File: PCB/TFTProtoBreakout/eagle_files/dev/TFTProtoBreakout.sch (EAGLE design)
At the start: 13 parts, among them SW1 PCM12SMTR, SW2 PCM12SMTR, SW3 PCM12SMTR, SW4 PCM12SMTR

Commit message: Added first cut of trace routing to board design. A bit messy, but functional.
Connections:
- removed net LEDA: C1.1, JP1.20, JP2.1, JP7.2
- net VCC: now also C1.1, JP1.20, JP2.1, JP7.2
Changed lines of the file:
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@@
-</segment>
-</net>
-<net name="LEDA" class="0">
-<segment>
-<pinref part="JP2" gate="G$1" pin="1"/>
-<wire x1="43.18" y1="5.08" x2="35.56" y2="5.08" width="0.1524" layer="91"/>
-<wire x1="35.56" y1="5.08" x2="35.56" y2="20.32" width="0.1524" layer="91"/>
-<pinref part="JP1" gate="G$1" pin="20"/>
-<wire x1="43.18" y1="22.86" x2="38.1" y2="22.86" width="0.1524" layer="91"/>
-<wire x1="38.1" y1="22.86" x2="38.1" y2="20.32" width="0.1524" layer="91"/>
-<wire x1="38.1" y1="20.32" x2="38.1" y2="17.78" width="0.1524" layer="91"/>
-<wire x1="38.1" y1="17.78" x2="63.5" y2="17.78" width="0.1524" layer="91"/>
-<wire x1="63.5" y1="17.78" x2="63.5" y2="22.86" width="0.1524" layer="91"/>
-<wire x1="63.5" y1="22.86" x2="81.28" y2="22.86" width="0.1524" layer="91"/>
-<wire x1="81.28" y1="22.86" x2="81.28" y2="20.32" width="0.1524" layer="91"/>
-<pinref part="JP7" gate="G$1" pin="2"/>
-<wire x1="81.28" y1="20.32" x2="81.28" y2="15.24" width="0.1524" layer="91"/>
-<wire x1="81.28" y1="15.24" x2="76.2" y2="15.24" width="0.1524" layer="91"/>
-<wire x1="35.56" y1="20.32" x2="38.1" y2="20.32" width="0.1524" layer="91"/>
-<pinref part="C1" gate="G$1" pin="1"/>
-<wire x1="88.9" y1="17.78" x2="88.9" y2="20.32" width="0.1524" layer="91"/>
-<wire x1="88.9" y1="20.32" x2="81.28" y2="20.32" width="0.1524" layer="91"/>
 </segment>
 </net>
@@
 <wire x1="-38.1" y1="-10.16" x2="-45.72" y2="-10.16" width="0.1524" layer="91"/>
 </segment>
+<segment>
+<pinref part="JP2" gate="G$1" pin="1"/>
+<wire x1="43.18" y1="5.08" x2="35.56" y2="5.08" width="0.1524" layer="91"/>
+<wire x1="35.56" y1="5.08" x2="35.56" y2="20.32" width="0.1524" layer="91"/>
+<pinref part="JP1" gate="G$1" pin="20"/>
+<wire x1="43.18" y1="22.86" x2="38.1" y2="22.86" width="0.1524" layer="91"/>
+<wire x1="38.1" y1="22.86" x2="38.1" y2="20.32" width="0.1524" layer="91"/>
+<wire x1="38.1" y1="20.32" x2="38.1" y2="17.78" width="0.1524" layer="91"/>
+<wire x1="38.1" y1="17.78" x2="63.5" y2="17.78" width="0.1524" layer="91"/>
+<wire x1="63.5" y1="17.78" x2="63.5" y2="22.86" width="0.1524" layer="91"/>
+<wire x1="63.5" y1="22.86" x2="81.28" y2="22.86" width="0.1524" layer="91"/>
+<wire x1="81.28" y1="22.86" x2="81.28" y2="20.32" width="0.1524" layer="91"/>
+<pinref part="JP7" gate="G$1" pin="2"/>
+<wire x1="81.28" y1="20.32" x2="81.28" y2="15.24" width="0.1524" layer="91"/>
+<wire x1="81.28" y1="15.24" x2="76.2" y2="15.24" width="0.1524" layer="91"/>
+<wire x1="35.56" y1="20.32" x2="38.1" y2="20.32" width="0.1524" layer="91"/>
+<pinref part="C1" gate="G$1" pin="1"/>
+<wire x1="88.9" y1="17.78" x2="88.9" y2="20.32" width="0.1524" layer="91"/>
+<wire x1="88.9" y1="20.32" x2="81.28" y2="20.32" width="0.1524" layer="91"/>
+</segment>
 </net>

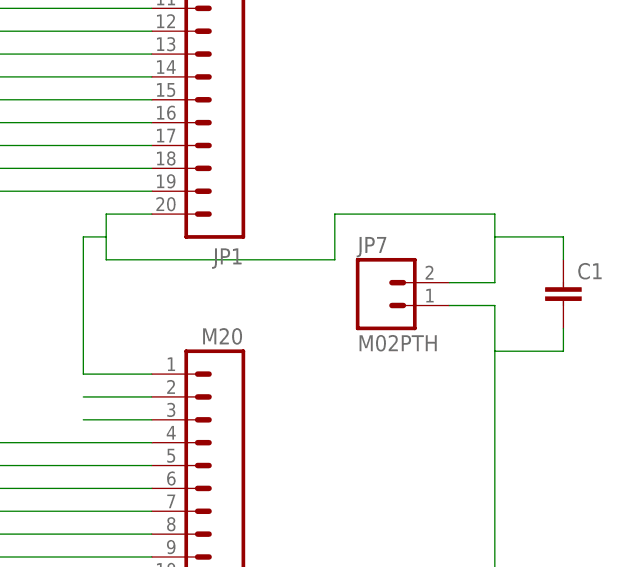
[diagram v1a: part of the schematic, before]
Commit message: Finalize routing to be more clean. Add keyhole for Power connections and Add labels.
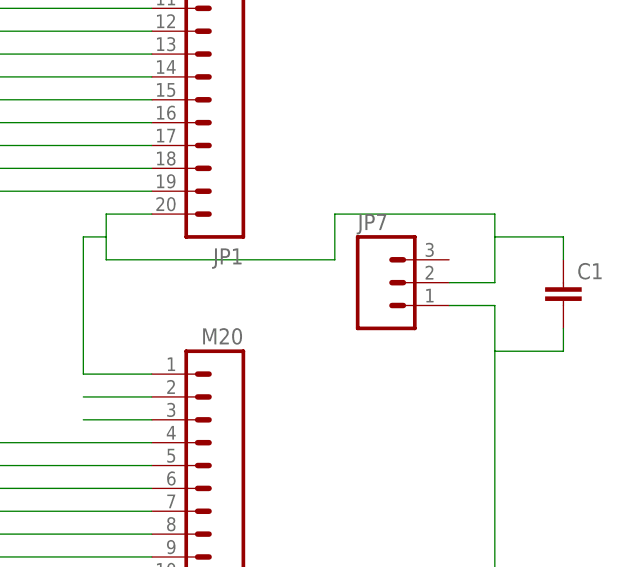
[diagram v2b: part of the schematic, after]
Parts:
- JP7: value M02PTH -> (none); device SparkFun-Connectors:M02PTH -> SparkFun-Connectors:M03PTH
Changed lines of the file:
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@@
 <part name="JP5" library="SparkFun-Connectors" deviceset="M03" device="PTH"/>
 <part name="JP6" library="SparkFun-Connectors" deviceset="M09" device=""/>
-<part name="JP7" library="SparkFun-Connectors" deviceset="M02" device="PTH"/>
 <part name="R1" library="SparkFun-Resistors" deviceset="1KOHM1/10W1%(0603)" device="" value="1K"/>
 <part name="SW1" library="freddyLibr" deviceset="PCM12SMTR" device=""/>
@@
 <part name="SW4" library="freddyLibr" deviceset="PCM12SMTR" device=""/>
 <part name="C1" library="SparkFun-Capacitors" deviceset="CAP" device="0805"/>
+<part name="JP7" library="SparkFun-Connectors" deviceset="M03" device="PTH"/>
 </parts>
 <sheets>
@@
 <instance part="JP5" gate="G$1" x="-15.24" y="-30.48"/>
 <instance part="JP6" gate="G$1" x="-2.54" y="-12.7"/>
-<instance part="JP7" gate="G$1" x="68.58" y="12.7"/>
 <instance part="R1" gate="G$1" x="30.48" y="71.12" rot="R180"/>
 <instance part="SW1" gate="G$1" x="-30.48" y="33.02" rot="R90"/>
@@
 <instance part="SW4" gate="G$1" x="-30.48" y="-12.7" rot="R90"/>
 <instance part="C1" gate="G$1" x="88.9" y="12.7"/>
+<instance part="JP7" gate="G$1" x="68.58" y="15.24"/>
 </instances>
 <busses>
@@
 <wire x1="38.1" y1="-50.8" x2="81.28" y2="-50.8" width="0.1524" layer="91"/>
 <wire x1="81.28" y1="-50.8" x2="81.28" y2="7.62" width="0.1524" layer="91"/>
-<pinref part="JP7" gate="G$1" pin="1"/>
 <wire x1="81.28" y1="7.62" x2="81.28" y2="12.7" width="0.1524" layer="91"/>
-<wire x1="81.28" y1="12.7" x2="76.2" y2="12.7" width="0.1524" layer="91"/>
 <label x="40.64" y="-50.8" size="1.778" layer="95"/>
 <pinref part="C1" gate="G$1" pin="2"/>
 <wire x1="88.9" y1="10.16" x2="88.9" y2="7.62" width="0.1524" layer="91"/>
 <wire x1="88.9" y1="7.62" x2="81.28" y2="7.62" width="0.1524" layer="91"/>
+<pinref part="JP7" gate="G$1" pin="1"/>
+<wire x1="81.28" y1="12.7" x2="76.2" y2="12.7" width="0.1524" layer="91"/>
 </segment>
 <segment>
@@
 <wire x1="63.5" y1="22.86" x2="81.28" y2="22.86" width="0.1524" layer="91"/>
 <wire x1="81.28" y1="22.86" x2="81.28" y2="20.32" width="0.1524" layer="91"/>
-<pinref part="JP7" gate="G$1" pin="2"/>
 <wire x1="81.28" y1="20.32" x2="81.28" y2="15.24" width="0.1524" layer="91"/>
-<wire x1="81.28" y1="15.24" x2="76.2" y2="15.24" width="0.1524" layer="91"/>
 <wire x1="35.56" y1="20.32" x2="38.1" y2="20.32" width="0.1524" layer="91"/>
 <pinref part="C1" gate="G$1" pin="1"/>
 <wire x1="88.9" y1="17.78" x2="88.9" y2="20.32" width="0.1524" layer="91"/>
 <wire x1="88.9" y1="20.32" x2="81.28" y2="20.32" width="0.1524" layer="91"/>
-</segment>
-</net>
+<pinref part="JP7" gate="G$1" pin="2"/>
+<wire x1="81.28" y1="15.24" x2="76.2" y2="15.24" width="0.1524" layer="91"/>
+</segment>
+</net>
